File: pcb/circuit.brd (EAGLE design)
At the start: 80 x 70 mm, 154 parts, among them IC1 MCP1612-ADJI/MS, IC2 MCP73833-AMI/UN-ND, IC3 WE-TVS, IC4 MCP3423, IC5 ATWINC1510-MR210PB1952-ND, IC6 MAX3378EEUD, IC7 RN4870, IC8 ATSAML22N18A, J2 22-05-7038-03, J3 22-05-7048-04, Q1 ECX-1210, T1 PMOS, T10 NMOSSOT323, T11 NMOSSOT323, T12 NMOSSOT323, T13 PMOS, T14 NMOSSOT323, T2 NMOSSOT323, T3 NMOSSOT323, T4 NMOSSOT323, T5 NMOSSOT323, T6 NMOSSOT323, T7 NMOSSOT323, T8 NMOSSOT323, T9 NMOSSOT323, X1 USB2-MICRO, X10 2.5MM-AUDIO-JACK-MONONO_DRILL, X11 2.5MM-AUDIO-JACK-MONONO_DRILL, X12 2.5MM-AUDIO-JACK-MONONO_DRILL, X13 2.5MM-AUDIO-JACK-MONONO_DRILL, X14 MOLEX_1MM_FPC, X15 IGRID-20, X2 B3S-1000, X3 JTAG-EDGE-CON, X4 2.5MM-AUDIO-JACK-MONODRILL, X5 2.5MM-AUDIO-JACK-MONODRILL, X6 2.5MM-AUDIO-JACK-MONODRILL, X7 2.5MM-AUDIO-JACK-MONODRILL, X8 2.5MM-AUDIO-JACK-MONODRILL, X9 2.5MM-AUDIO-JACK-MONONO_DRILL

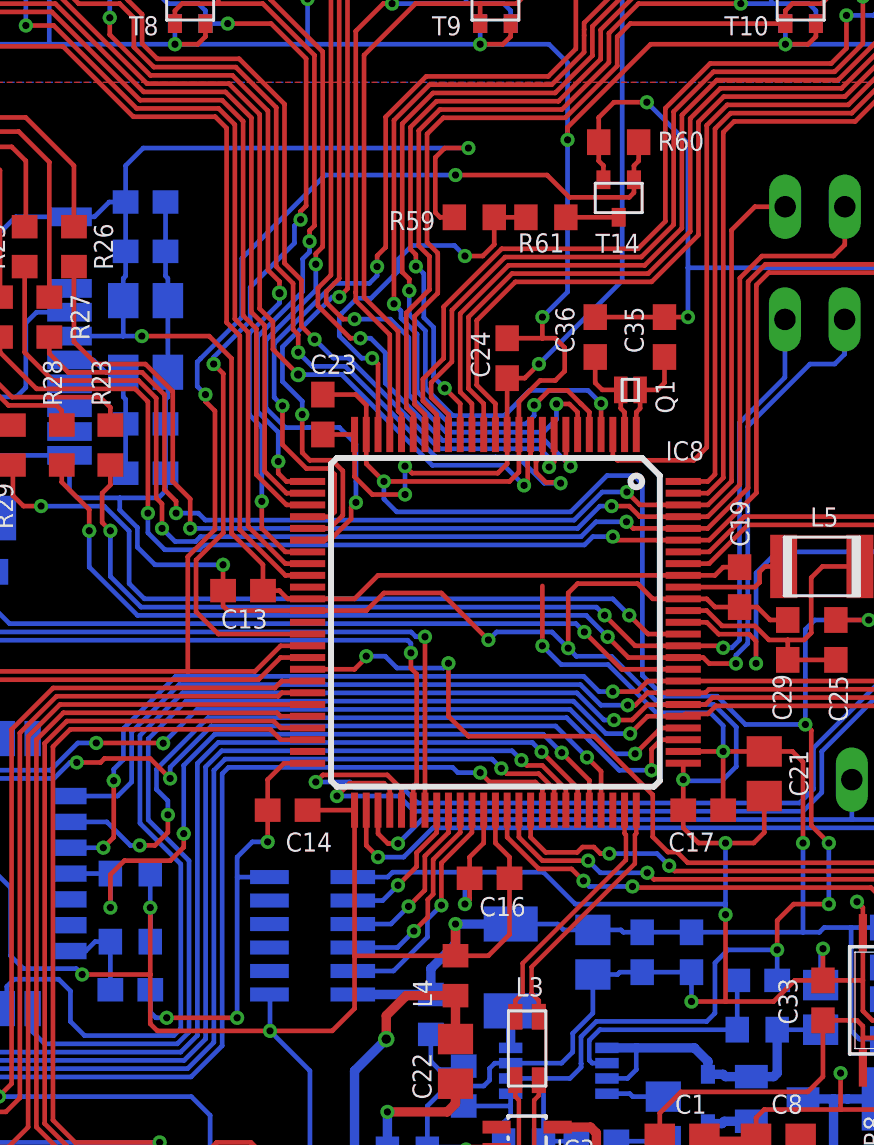
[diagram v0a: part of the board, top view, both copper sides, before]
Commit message: updated 3d Models
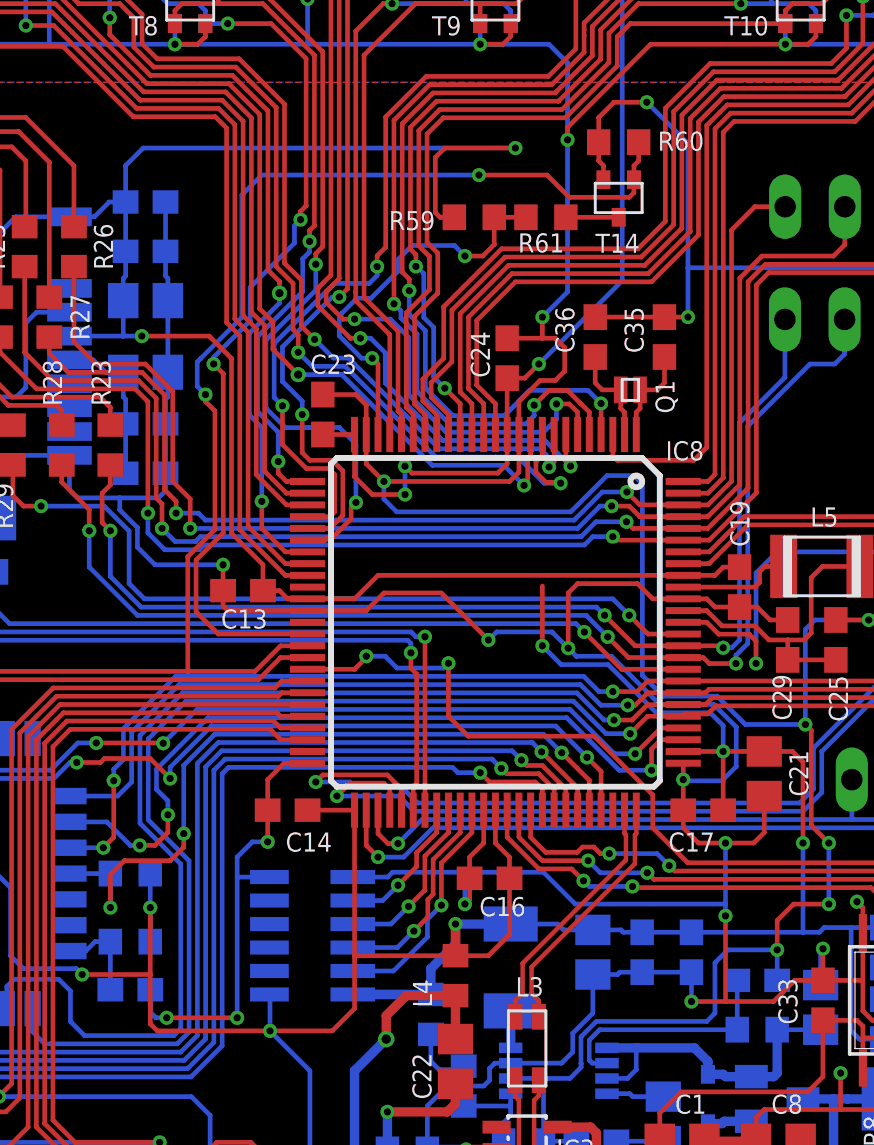
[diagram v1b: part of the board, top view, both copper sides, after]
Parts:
- L1: device Thermo_Library:WE-LHMI -> thermo:WE-LHMI
- L4: device Thermo_Library:L0603 -> thermo:L0603
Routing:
- net +3V3: track 295.9 -> 299.9 mm
- net SENSOR_INTERN_EN: track 64.9 -> 66.5 mm

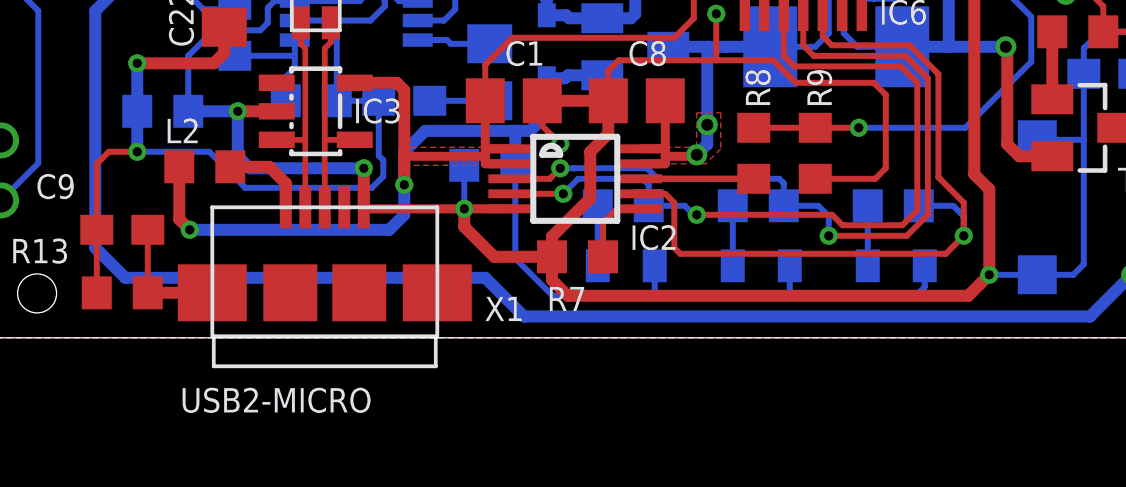
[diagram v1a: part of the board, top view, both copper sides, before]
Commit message: LED Footprint changed
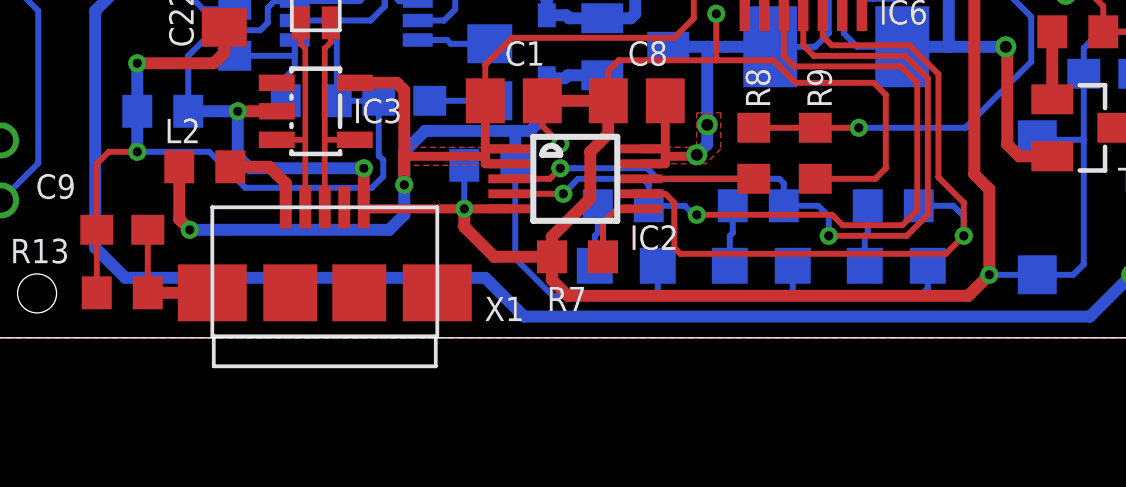
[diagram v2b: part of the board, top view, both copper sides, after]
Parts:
- D1, D2, D3: device Thermo_Library:LED_2012 -> thermo:LED_2012
- D4: device Thermo_Library:SOD323 -> thermo:SOD323
- J2: device con-molex:7395-03 -> thermo:7395-03
- J3: device con-molex:7395-04 -> thermo:7395-04
- L2: value (none) -> L-0603; device Thermo_Library:L0603 -> thermo:L0603
- L4: value (none) -> L-0603
- L5: device Thermo_Library:L-1210 -> thermo:L-1210
- X2: device Thermo_Library:B3S -> thermo:B3S
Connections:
- net RES1 renamed RES0
